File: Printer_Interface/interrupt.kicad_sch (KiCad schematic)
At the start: 15 parts, among them J3 IACK, J4 IRQ, U16 74HCT138, U17 INTERRUPT_GAL, U18 74HCT1G32, U19 74LVC1G08, U20 74LVC1G175, U21 74LVC1G74, U22 74LVC1G07

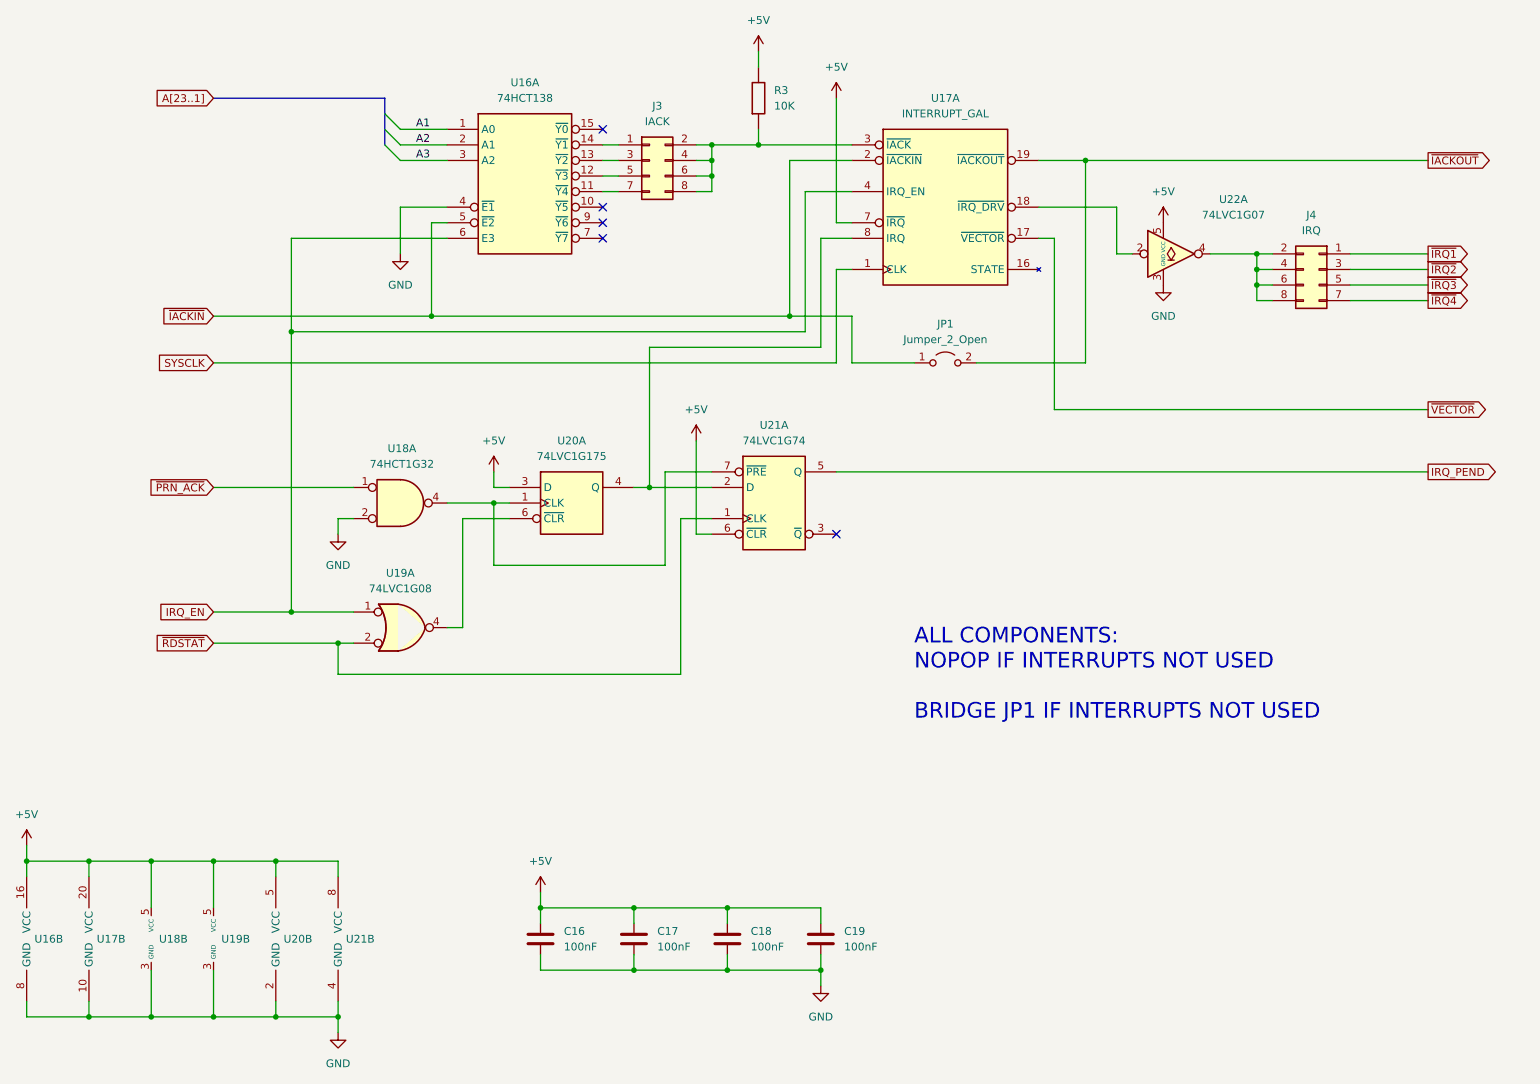
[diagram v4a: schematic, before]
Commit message: Interrupt logic changes
* Changed to a dual DFF package which removes 3 individual parts
* Verified that the logic is PC compatible
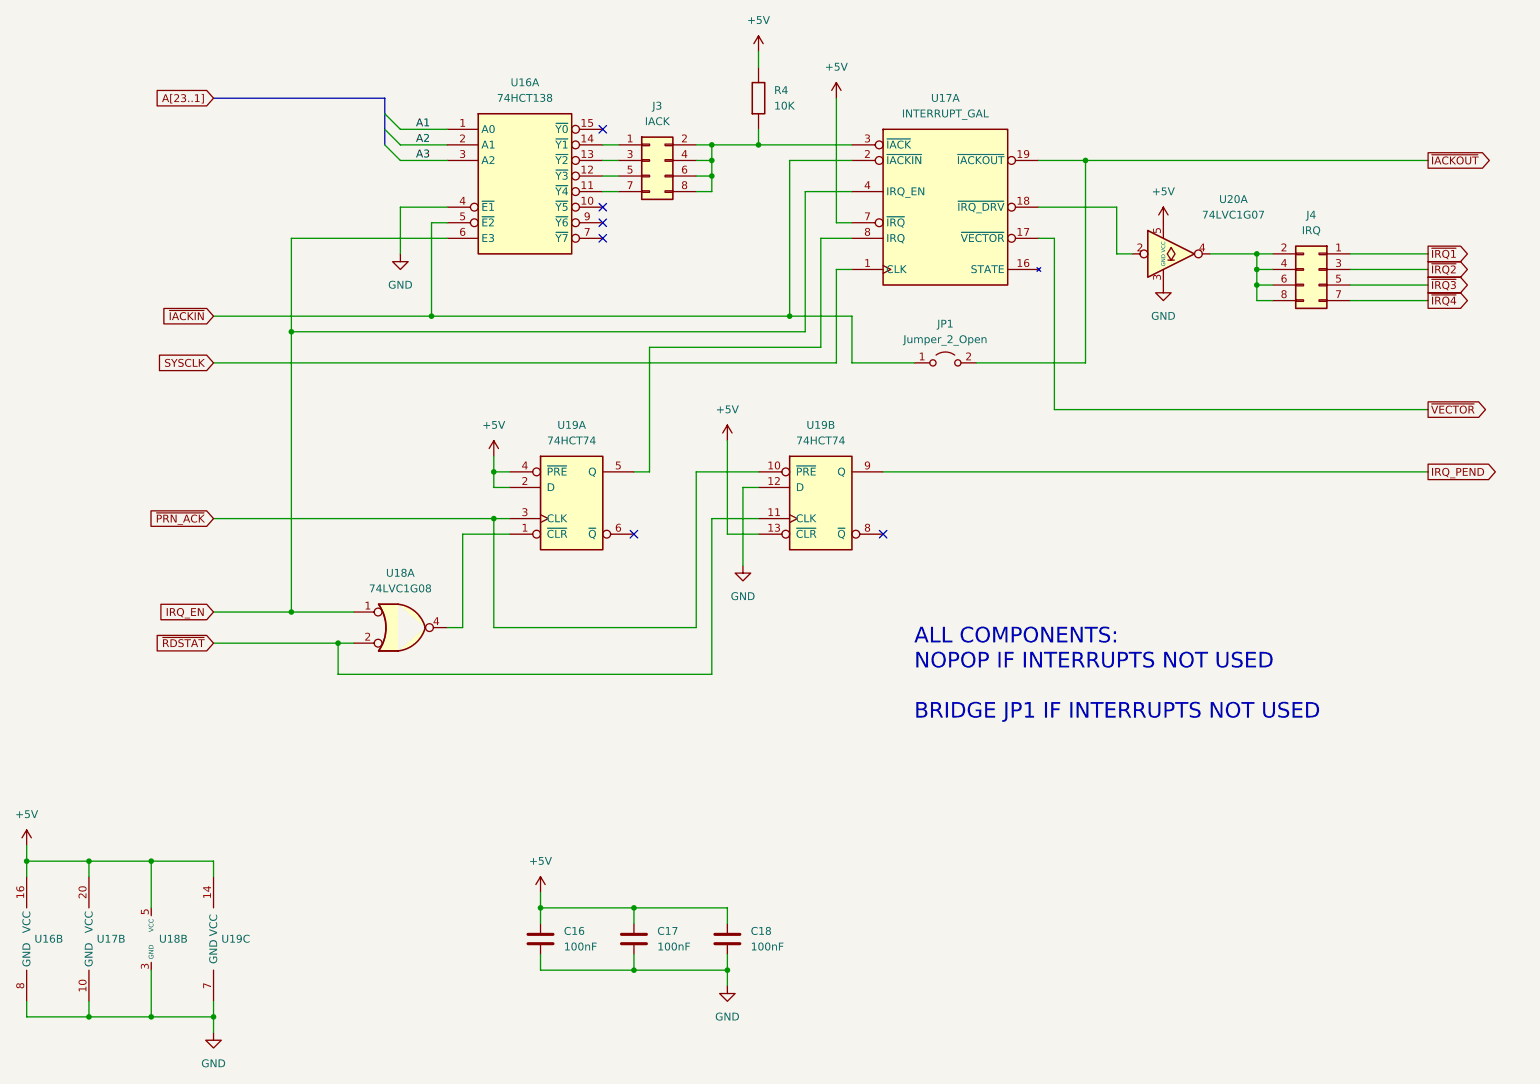
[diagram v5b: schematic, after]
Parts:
- removed C19: 100nF, COMET_footprints:C_SMD0805, symbol COMET_symbols:C
- removed U18: 74HCT1G32, COMET_footprints:Package_SOT23-5, symbol COMET_symbols:74x1G32
- removed U20: 74LVC1G175, COMET_footprints:Package_SOT23-6, symbol COMET_symbols:74x1G175
- removed U21: 74LVC1G74, COMET_footprints:Package_TSSOP-8_3x3mm_P0.65mm, symbol COMET_symbols:74x1G74
- added U19: 74HCT74, COMET_footprints:Package_SO14, symbol COMET_symbols:74x74
- renumbered R3 to R4, U19 to U18, U22 to U20
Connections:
- net +5V: now also U19.13 (~{CLR}), U19.14 (VCC), U19.2 (D), U19.4 (~{PRE})
- net GND: now also U19.12 (D), U19.7 (GND)
- net IRQ_PEND: now also U19.9 (Q)
- net ~{PRN_ACK}: now also U19.10 (~{PRE}), U19.3 (CLK)
- net ~{RDSTAT}: now also U19.11 (CLK)
- net at U18.4: now also U19.1 (~{CLR})
- net at U17.8 (IRQ): now also U19.5 (Q)
- no-connect marks 5 -> 6
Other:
- moved on the sheet: U18B
